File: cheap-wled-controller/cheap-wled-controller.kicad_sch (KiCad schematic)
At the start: 6 parts, among them CN1 WJ124-3.81-5P-14-00A, U1 AMS1117-3.3, U2 ESP32-S3-WROOM-1-N4R2, U3 ZX-PZ2.0-2-5PZZ, U4 74LV1T34GWH_C5199768

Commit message: voltage selector
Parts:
- added C1: 1u, cheap-wled-controller:C0805, symbol easyeda:0805B105K500NT_C215803
- added R1: 1k, cheap-wled-controller:R0805, symbol easyeda:0805W8F1001T5E
- added R2: 10k, cheap-wled-controller:R0805, symbol easyeda:0805W8F1002T5E
- added R3: 6.8k, cheap-wled-controller:R0805, symbol easyeda:0805W8F6801T5E
- added R4: 24K, cheap-wled-controller:R0805, symbol easyeda:0805W8F2402T5E
- added R5: 56K, cheap-wled-controller:R0805, symbol easyeda:0805W8F5602T5E
- added U5: CH224K, cheap-wled-controller:ESSOP-10_L4.9-W3.9-P1.0-LS6.0-TL-EP, symbol easyeda:CH224K
- U3: value ZX-PZ2.0-2-5PZZ -> VOLTAGE SELECT
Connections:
- net GND: now also C1.2, R3.1, U5.11 (GND)
- net at USBC1.A5 (CC1): now also U5.7 (CC1)
- net at USBC1.B1 (GND): now also USBC1.B4 (VBUS), R1.1, R2.2
- net at USBC1.B5 (CC2): now also U5.6 (CC2)
- net VDD_C: now reaches U3.10
- net VDD_C: now also C1.1, R1.2, U5.1 (VDD)
- net at U3.3: now also U3.5, U3.7, U3.9, U5.9 (CFG1)
- net at U3.4: now also R5.2
- net at U3.6: now also R4.2
- net at U3.8: now also R3.2
- new net: R2.1, U5.8 (VBUS)
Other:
- moved on the sheet: U3

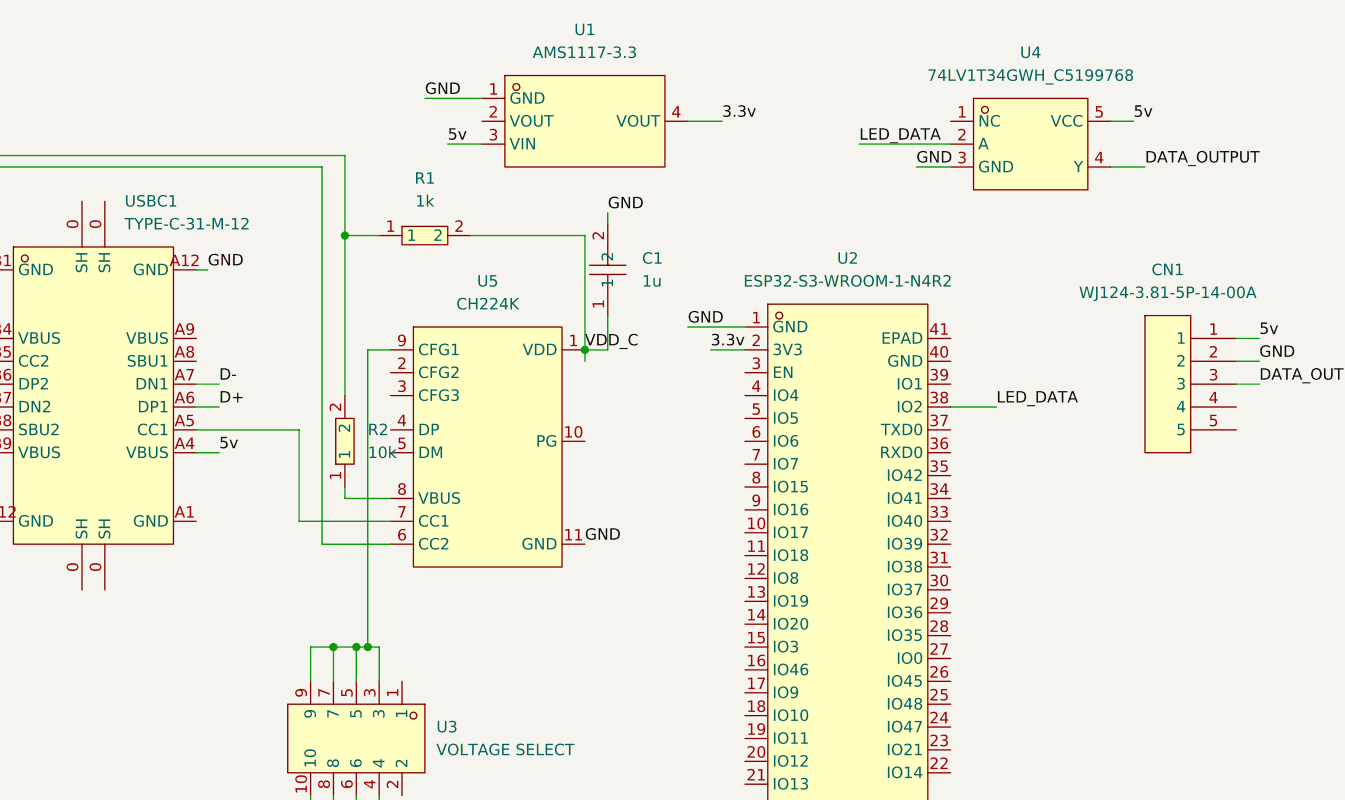
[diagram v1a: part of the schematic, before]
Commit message: footprint problem solved
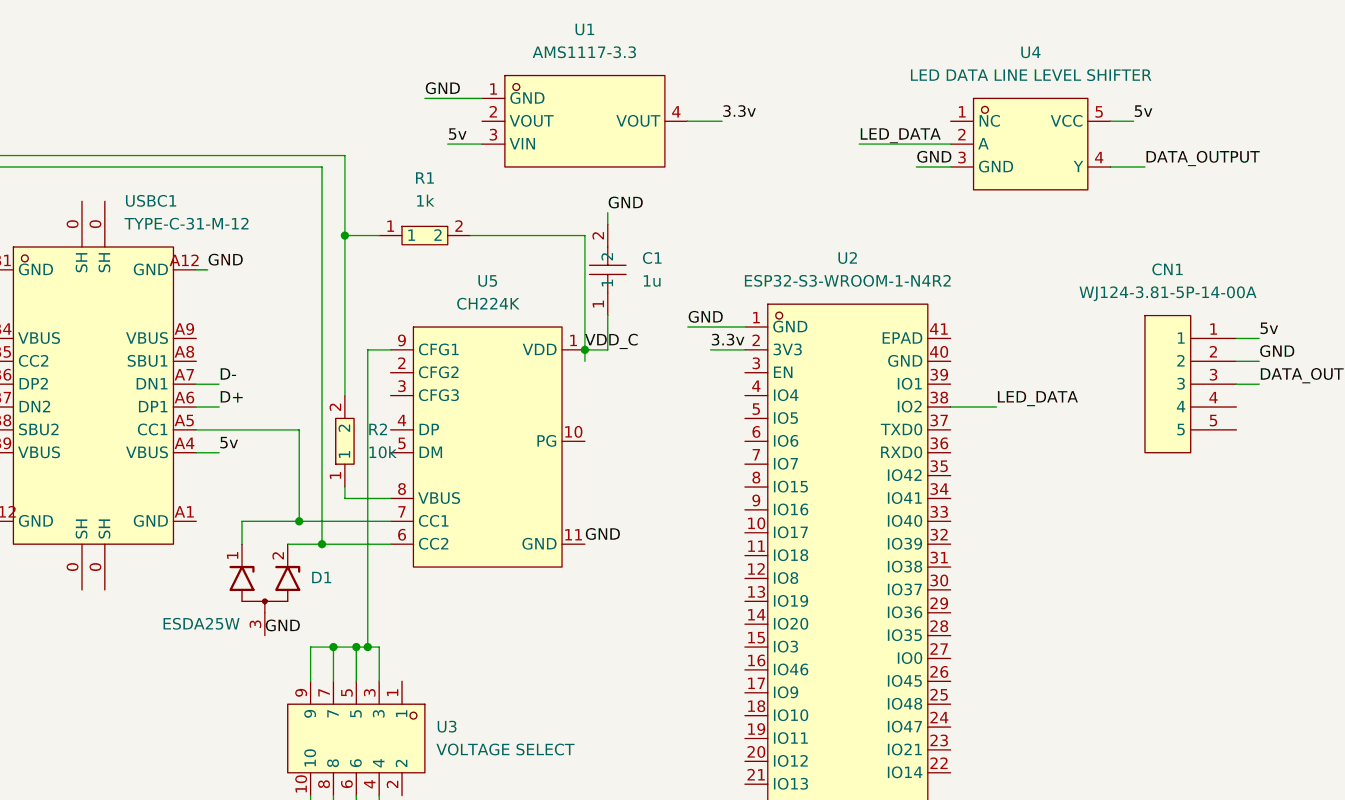
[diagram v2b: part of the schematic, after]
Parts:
- added D1: ESDA25W, Package_TO_SOT_SMD:SOT-323_SC-70, symbol Power_Protection:RCLAMP0502BA
- U4: value 74LV1T34GWH_C5199768 -> LED DATA LINE LEVEL SHIFTER
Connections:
- net GND: now also D1.3 (A)
- net at U5.7 (CC1), USBC1.A5 (CC1): now also D1.1 (K1)
- net at U5.6 (CC2), USBC1.B5 (CC2): now also D1.2 (K2)
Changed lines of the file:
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@@
+	)
+	(junction
+		(at 77.47 97.79)
+		(diameter 0)
+		(color 0 0 0 0)
 	)
 	(junction
@@
 		(color 0 0 0 0)
 	)
+	(junction
+		(at 80.01 100.33)
+		(diameter 0)
+		(color 0 0 0 0)
+	)
 	(wire
 		(pts
@@
 	(wire
 		(pts
+			(xy 71.12 100.33) (xy 71.12 97.79)
+		)
+		(stroke
+			(width 0)
+			(type default)
+		)
+	)
+	(wire
+		(pts
 			(xy 109.22 78.74) (xy 111.76 78.74)
 		)
@@
 	(wire
 		(pts
+			(xy 71.12 97.79) (xy 77.47 97.79)
+		)
+		(stroke
+			(width 0)
+			(type default)
+		)
+	)
+	(wire
+		(pts
 			(xy 81.28 128.27) (xy 81.28 130.81)
 		)
@@
 		(pts
 			(xy 82.55 66.04) (xy 86.36 66.04)
+		)
+		(stroke
+			(width 0)
+			(type default)
+		)
+	)
+	(wire
+		(pts
+			(xy 76.2 100.33) (xy 80.01 100.33)
 		)
 		(stroke
@@
 	(label "DATA_OUTPUT"
 		(at 171.45 58.42 0)
+		(effects
+			(font
+				(size 1.27 1.27)
+			)
+			(justify left bottom)
+		)
+	)
+	(label "GND"
+		(at 73.66 110.49 0)
 		(effects
 			(font
@@
 	)
 	(symbol
+		(lib_id "Power_Protection:RCLAMP0502BA")
+		(at 73.66 105.41 90)
+		(unit 1)
+		(exclude_from_sim no)
+		(in_bom yes)
+		(on_board yes)
+		(dnp no)
+		(property "Reference" "D1"
+			(at 78.74 104.0765 90)
+			(effects
+				(font
+					(size 1.27 1.27)
+				)
+				(justify right)
+			)
+		)
+		(property "Value" "ESDA25W"
+			(at 62.23 109.22 90)
+			(effects
+				(font
+					(size 1.27 1.27)
+				)
+				(justify right)
+			)
+		)
+		(property "Footprint" "Package_TO_SOT_SMD:SOT-323_SC-70"
+			(at 81.28 105.41 0)
+			(effects
+				(font
+					(size 1.27 1.27)
+				)
+				(hide yes)
+			)
+		)
+		(property "Datasheet" "https://www.semtech.com/products/circuit-protection/low-capacitance/rclamp0502ba"
+			(at 71.12 104.14 0)
+			(effects
+				(font
+					(size 1.27 1.27)
+				)
+				(hide yes)
+			)
+		)
+		(property "Description" ""
+			(at 73.66 105.41 0)
+			(effects
+				(font
+					(size 1.27 1.27)
+				)
+				(hide yes)
+			)
+		)
+		(property "LCSC" "C3021136"
+			(at 73.66 105.41 90)
+			(effects
+				(font
+					(size 1.27 1.27)
+				)
+				(hide yes)
+			)
+		)
+		(pin "3"
+		)
+		(pin "1"
+		)
+		(pin "2"
+		)
+		(instances
+			(project "cheap-wled-controller"
+				(path "/6a5d3644-22ac-4961-ba70-9807615c046f"
+					(reference "D1")
+					(unit 1)
+				)
+			)
+		)
+	)
+	(symbol
 		(lib_id "easyeda:0805W8F1002T5E")
 		(at 82.55 88.9 90)
@@
 			)
 		)
-		(property "Value" "74LV1T34GWH_C5199768"
+		(property "Value" "LED DATA LINE LEVEL SHIFTER"
 			(at 158.75 48.26 0)
 			(effects

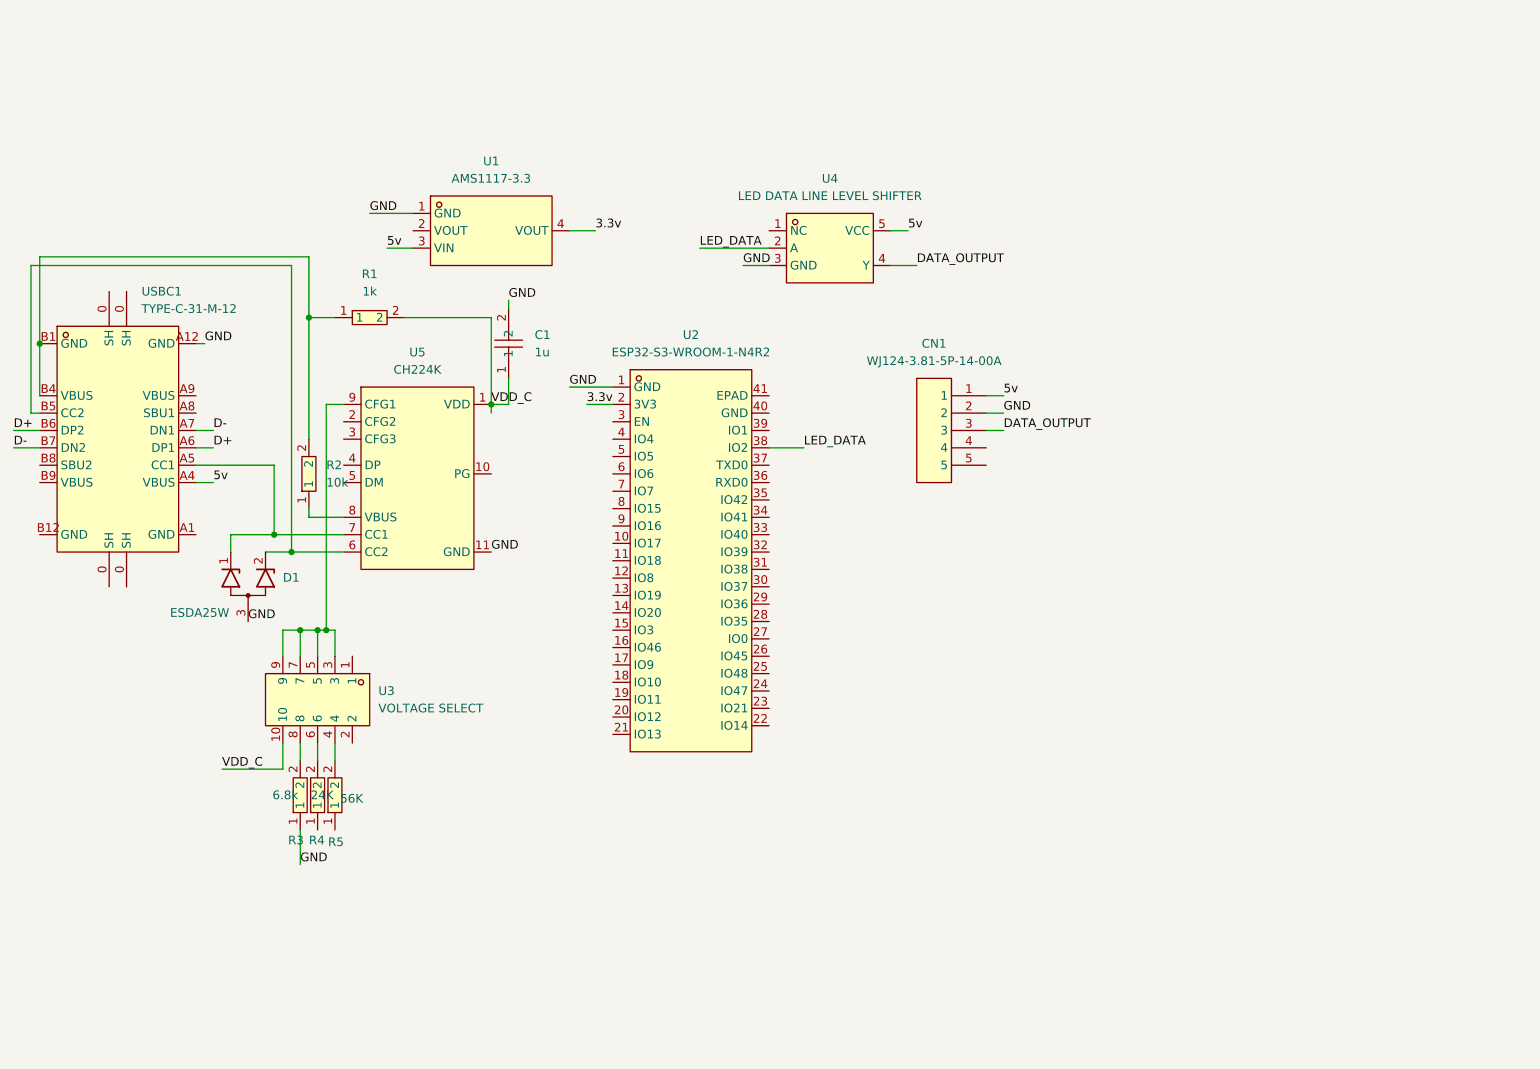
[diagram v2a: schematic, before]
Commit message: etapa de 5v a 3v
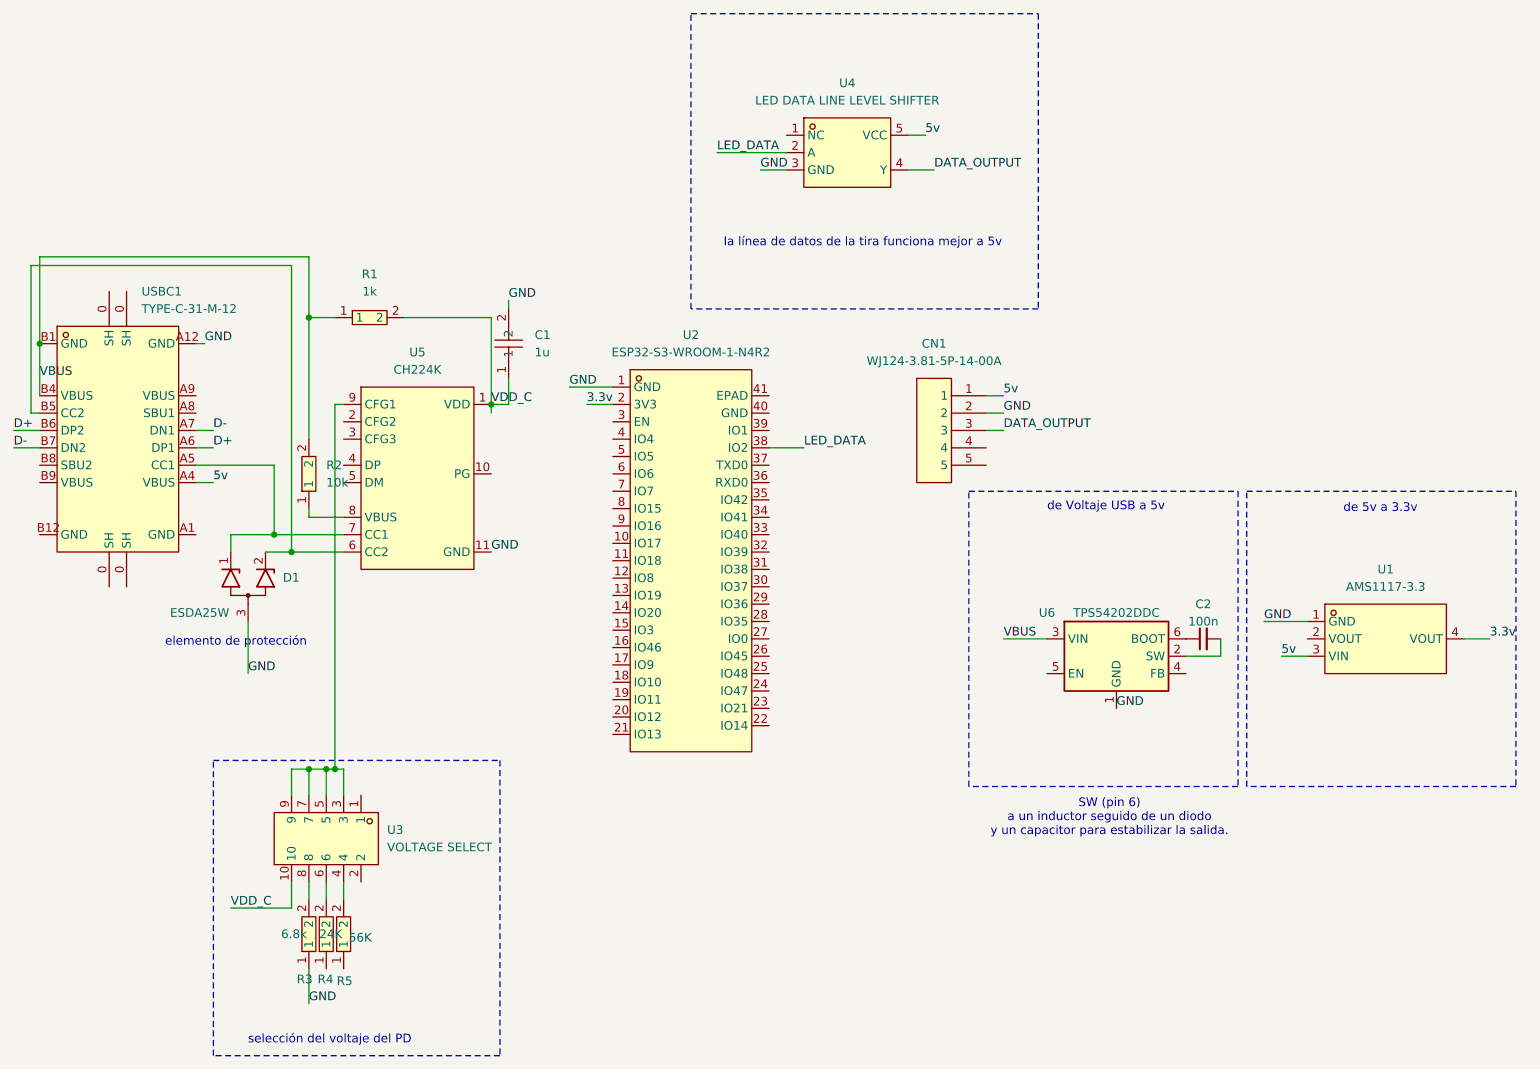
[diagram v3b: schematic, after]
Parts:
- added C2: 100n, Capacitor_SMD:C_0603_1608Metric, symbol Device:C_Small
- added U6: TPS54202DDC, Package_TO_SOT_SMD:SOT-23-6, symbol Regulator_Switching:TPS54202DDC
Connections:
- net GND: now also U6.1 (GND)
- net VBUS: now reaches R1.1, R2.2, USBC1.B1 (GND), USBC1.B4 (VBUS)
- net VBUS: now also U6.3 (VIN)
- new net: C2.2, U6.2 (SW)
- new net: C2.1, U6.6 (BOOT)
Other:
- note added: "SW (pin 6) a un inductor seguido de un diodo y un capacitor para estabilizar la salida."
- note added: "de 5v a 3.3v"
- note added: "de Voltaje USB a 5v"
- note added: "elemento de protección"
- note added: "la línea de datos de la tira funciona mejor a 5v"
- note added: "selección del voltaje del PD"
- moved on the sheet: R3, R4, R5, U1, U3, U4

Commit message: fusible
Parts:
- added D2, D3: LED_Small, LED_SMD:LED_0603_1608Metric, symbol Device:LED_Small
- added F1: DIR, YULC:FUSE-TH_XF-508P-A-B, symbol Device:Fuse_Small
- added R6, R7: 10k, Resistor_SMD:R_0603_1608Metric, symbol Device:R_Small
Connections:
- net 3.3v: now also R6.2
- net 5v: now also C2.2, U6.2 (SW); no longer CN1.1, USBC1.A4 (VBUS)
- net GND: now also D2.1 (K), D3.1 (K)
- net VBUS: now also F1.1
- new net: D3.2 (A), R7.1
- new net: D2.2 (A), R6.1
- new net VLED: CN1.1, F1.2

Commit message: refactor using 0805 components
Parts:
- removed C1: 1u, cheap-wled-controller:C0805, symbol easyeda:0805B105K500NT_C215803
- removed C2: 100n, Capacitor_SMD:C_0603_1608Metric, symbol Device:C_Small
- removed CN1: WJ124-3.81-5P-14-00A, cheap-wled-controller:CONN-TH_5P-P3.81_KF124-3.81-5P, symbol easyeda:WJ124-3.81-5P-14-00A
- removed D3: LED_Small, LED_SMD:LED_0603_1608Metric, symbol Device:LED_Small
- removed F1: DIR, YULC:FUSE-TH_XF-508P-A-B, symbol Device:Fuse_Small
- removed R1: 1k, cheap-wled-controller:R0805, symbol easyeda:0805W8F1001T5E
- removed R2: 10k, cheap-wled-controller:R0805, symbol easyeda:0805W8F1002T5E
- removed R3: 6.8k, cheap-wled-controller:R0805, symbol easyeda:0805W8F6801T5E
- removed R4: 24K, cheap-wled-controller:R0805, symbol easyeda:0805W8F2402T5E
- removed R5: 56K, cheap-wled-controller:R0805, symbol easyeda:0805W8F5602T5E
- removed R6, R7: 10k, Resistor_SMD:R_0603_1608Metric, symbol Device:R_Small
- removed U1: AMS1117-3.3, cheap-wled-controller:SOT-223-3_L6.5-W3.4-P2.30-LS7.0-BR, symbol easyeda:AMS1117-3.3
- removed U2: ESP32-S3-WROOM-1-N4R2, cheap-wled-controller:WIRELM-SMD_ESP32-S3-WROOM-1, symbol easyeda:ESP32-S3-WROOM-1-N4R2
- removed U3: VOLTAGE SELECT, cheap-wled-controller:HDR-TH_10P-P2.00-V-M-R2-C5-S2.00, symbol easyeda:ZX-PZ2.0-2-5PZZ
- removed U4: LED DATA LINE LEVEL SHIFTER, cheap-wled-controller:TSSOP-5_L2.0-W1.3-P0.65-LS2.1-BR, symbol easyeda:74LV1T34GWH_C5199768
- removed U5: CH224K, cheap-wled-controller:ESSOP-10_L4.9-W3.9-P1.0-LS6.0-TL-EP, symbol easyeda:CH224K
- removed U6: TPS54202DDC, Package_TO_SOT_SMD:SOT-23-6, symbol Regulator_Switching:TPS54202DDC
- removed USBC1: TYPE-C-31-M-12, cheap-wled-controller:USB-C_SMD-TYPE-C-31-M-12, symbol easyeda:TYPE-C-31-M-12
- added C1, C4, C5, C6: 10u, cheap-wled-controller:C0805, symbol easyeda:CL21A106KOQNNNE
- added C2: 1u, cheap-wled-controller:C0805, symbol easyeda:0805B105K500NT_C215803
- added C29: 100n, cheap-wled-controller:C0805, symbol easyeda:C0805B104K500NT
- added C3: 0.1u, cheap-wled-controller:C0805, symbol easyeda:C0805B104K500NT
- added C30: 56p, cheap-wled-controller:C0805, symbol easyeda:0805CG560J500NT
- added D3: ~, Diode_SMD:D_SMA, symbol Diode:SM6T6V8A
- added D4: LED_Small, LED_SMD:LED_0603_1608Metric, symbol Device:LED_Small
- added F2: DIR, YULC:FUSE-TH_XF-508P-A-B, symbol Device:Fuse_Small
- added H1, H2, H3: MountingHole, symbol Mechanical:MountingHole
- added J10: Conn_01x05_Pin, YULC:CONN-TH_5P-P3.81_KF124-3.81-5P, symbol Connector:Conn_01x05_Pin
- added J2: USB_C_Receptacle, Connector_USB:USB_C_Receptacle_G-Switch_GT-USB-7010ASV, symbol Connector:USB_C_Receptacle
- added J4: Conn_02x05_Odd_Even, Connector_PinHeader_2.00mm:PinHeader_2x05_P2.00mm_Vertical, symbol Connector_Generic:Conn_02x05_Odd_Even
- added J6: Conn_01x05_Pin, Connector_PinSocket_2.54mm:PinSocket_1x05_P2.54mm_Vertical, symbol Connector:Conn_01x05_Pin
- added J7: Conn_01x02_Pin, Connector_JST:JST_PH_B2B-PH-K_1x02_P2.00mm_Vertical, symbol Connector:Conn_01x02_Pin
- added J8: Conn_01x07_Pin, Connector_PinSocket_2.54mm:PinSocket_1x07_P2.54mm_Vertical, symbol Connector:Conn_01x07_Pin
- added L2: 4.7u, Inductor_SMD:L_1008_2520Metric, symbol Device:L
- added Q3: NMOS, YULC:DFN-8_L5.9-W5.2-P1.27-LS6.2-BL, symbol Simulation_SPICE:NMOS
- added R1, R9: 4k, cheap-wled-controller:R0805, symbol easyeda:ARG05FTC4001N
- added R10, R11, R12, R14, R4, R5: 10k, cheap-wled-controller:R0805, symbol easyeda:0805W8F1002T5E
- added R13, R22: 27k, cheap-wled-controller:R0805, symbol easyeda:RC0805FR-0727KL
- added R15, R2: 56k, cheap-wled-controller:R0805, symbol easyeda:0805W8F5602T5E
- added R16: 24k, cheap-wled-controller:R0805, symbol easyeda:0805W8F2402T5E
- added R17: 6.8k, cheap-wled-controller:R0805, symbol easyeda:0805W8F6801T5E
- added R20: 100k, cheap-wled-controller:R0805, symbol easyeda:0805W8F1003T5E_C149504
- added R3: 1k, cheap-wled-controller:R0805, symbol easyeda:0805W8F1001T5E
- added SW1: SW_Push, YULC:SW-SMD_TSA245G00D-250, symbol Switch:SW_Push
- added U1: USBLC6-2SC6, Package_TO_SOT_SMD:SOT-23-6, symbol Power_Protection:USBLC6-2SC6
- added U2: ESP32-S3-WROOM-1-N16R2, YULC:XCVR_ESP32-S3-WROOM-1-N16R2, symbol ESP32-S3-WROOM-1-N16R2:ESP32-S3-WROOM-1-N16R2
- added U3: CH224K, ch224k:ESSOP-10_L4.9-W3.9-P1.0-LS6.0-TL-EP, symbol 0my_project:CH224K
- added U4: MX5014S, YULC:SOIC-8_L4.9-W3.9-P1.27-LS6.0-BL, symbol horizontal_button:MX5014S
- added U7: TPS54202DDC, Package_TO_SOT_SMD:SOT-23-6, symbol Regulator_Switching:TPS54202DDC
- added U9: AMS1117-3.3, cheap-wled-controller:SOT-223-3_L6.5-W3.4-P2.30-LS7.0-BR, symbol easyeda:AMS1117-3.3
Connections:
- net D+: now also J2.A6 (D+), J2.B6 (D+), U1.3 (I/O2)
- net D-: now also J2.A7 (D-), J2.B7 (D-), U1.1 (I/O1)
- net GND: now also C1.1, C2.1, C3.1, C4.1, C5.1, C6.1, D3.2 (A2), D4.1 (K), J10.4 (Pin_4), J10.5 (Pin_5), J2.A1 (GND), J2.A12 (GND), J2.B1 (GND), J2.B12 (GND), J2.S1 (SHIELD), J6.4 (Pin_4), J7.2 (Pin_2), J8.4 (Pin_4), R11.1, R13.1, R16.1, R17.1, R2.1, R22.1, SW1.1, U1.2 (GND), U2.1 (GND), U2.40 (GND), U2.41_1 (GND), U2.41_2 (GND), U2.41_3 (GND), U2.41_4 (GND), U2.41_5 (GND), U2.41_6 (GND), U2.41_7 (GND), U2.41_8 (GND), U2.41_9 (GND), U3.0 (GND), U4.4 (GND), U7.1 (GND), U9.1 (GND)
- net LED_DATA: now also J10.3 (Pin_3), U2.39 (IO1)
- net VDD_C: now also C2.2, J4.9 (Pin_9), R3.1, R5.2, U3.1 (VDD)
- net at D2.2 (A): now also R14.1
- net at D1.1 (K1): now also J2.B5 (CC2), U3.6 (CC2)
- net at D1.2 (K2): now also J2.A5 (CC1), U3.7 (CC1)
- new net: R10.2, R15.1
- new net: R5.1, U3.10 (PG)
- new net: R4.1, U3.8 (VBUS)
- new net: D4.2 (A), R12.1
- new net: J4.5 (Pin_5), R16.2
- new net: R1.2, SW1.2, U2.27 (IO0)
- new net: C4.2, R9.2, U2.3 (EN)
- new net: J4.3 (Pin_3), R2.2
- new net: J4.10 (Pin_10), J4.4 (Pin_4), J4.6 (Pin_6), J4.8 (Pin_8), U3.9 (CFG1)
- new net: Q3.1 (G), U4.5 (Gate)
- new net: J4.7 (Pin_7), R17.2
- new net +3.3V: C3.2, C6.2, J6.5 (Pin_5), J8.1 (Pin_1), R1.1, R14.2, R9.1, U2.2 (3V3), U9.4 (VOUT)
- new net +5V: C30.2, J7.1 (Pin_1), L2.2, R20.2, U9.3 (VIN)
- new net BOOT: C29.2, U7.6 (BOOT)
- new net D+_OUT: U1.4 (I/O2), U2.14 (IO20)
- new net D-_OUT: U1.6 (I/O1), U2.13 (IO19)
- new net FB: C30.1, R13.2, R20.1, R22.2, U7.4 (FB)
- new net GPIO12: U2.12 (IO8)
- new net GPIO18: U2.11 (IO18)
- new net GPIO35: U2.28 (IO35)
- new net GPIO36: J8.7 (Pin_7), U2.29 (IO36)
- new net GPIO37: J8.6 (Pin_6), U2.30 (IO37)
- new net GPIO38: J8.5 (Pin_5), U2.31 (IO38)
- new net GPIO39: U2.32 (IO39)
- new net GPIO4: J6.3 (Pin_3), U2.4 (IO4)
- new net GPIO40: U2.33 (IO40)
- new net GPIO41: U2.34 (IO41)
- new net GPIO42: U2.35 (IO42)
- new net GPIO5: J6.2 (Pin_2), U2.5 (IO5)
- new net GPIO6: J6.1 (Pin_1), U2.6 (IO6)
- new net LED_1_VCC: J10.1 (Pin_1), J10.2 (Pin_2), Q3.3 (S), U4.3 (Source)
- new net MOS_1: U2.24 (IO47), U4.2 (Input)
- new net MOS_2: U2.23 (IO21)
- new net OUT: R12.2
- new net RX: J8.3 (Pin_3), U2.36 (RXD0)
- new net SW_5V: C29.1, L2.1, U7.2 (SW)
- new net TX: J8.2 (Pin_2), U2.37 (TXD0)
- new net VBUS_C: C5.2, D3.1 (A1), F2.1, J2.A4 (VBUS), J2.A9 (VBUS), J2.B4 (VBUS), J2.B9 (VBUS), R3.2, R4.2, U7.3 (VIN)
- new net VOLT_OUT: R10.1, R11.2, U2.7 (IO7)
- new net V_LED: C1.2, F2.2, Q3.2 (D), R15.2, U4.1 (V+)
- no-connect marks 0 -> 33
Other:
- note added: "3.3V LDO REGULATOR"
- note added: "5-9-12-15-20V"
- note added: "5V BUCK REGULATOR"
- note added: "ESP32-S3 + LED MOSFET"
- note added: "PD VOLTAGE SELECTOR"
- note added: "POWER STATUS LED"
- note added: "USB-C + PD IC"
- note removed: "SW (pin 6) a un inductor seguido de un diodo y un capacitor para estabilizar la salida."
- note removed: "de 5v a 3.3v"
- note removed: "de Voltaje USB a 5v"
- note removed: "elemento de protección"
- note removed: "la línea de datos de la tira funciona mejor a 5v"
- note removed: "selección del voltaje del PD"
